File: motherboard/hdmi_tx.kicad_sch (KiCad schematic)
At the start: 38 parts, among them J8 HDMI_A, Q1 2SK3018W, Q2 2SK3018W, Q3 L2N7002WT1G, Q4 2SK3018W, Q5 2SK3018W, Q6 WNM6002-3/TR, Q7 WNM6002-3/TR, Q8 WNM6002-3/TR, Q9 WNM6002-3/TR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

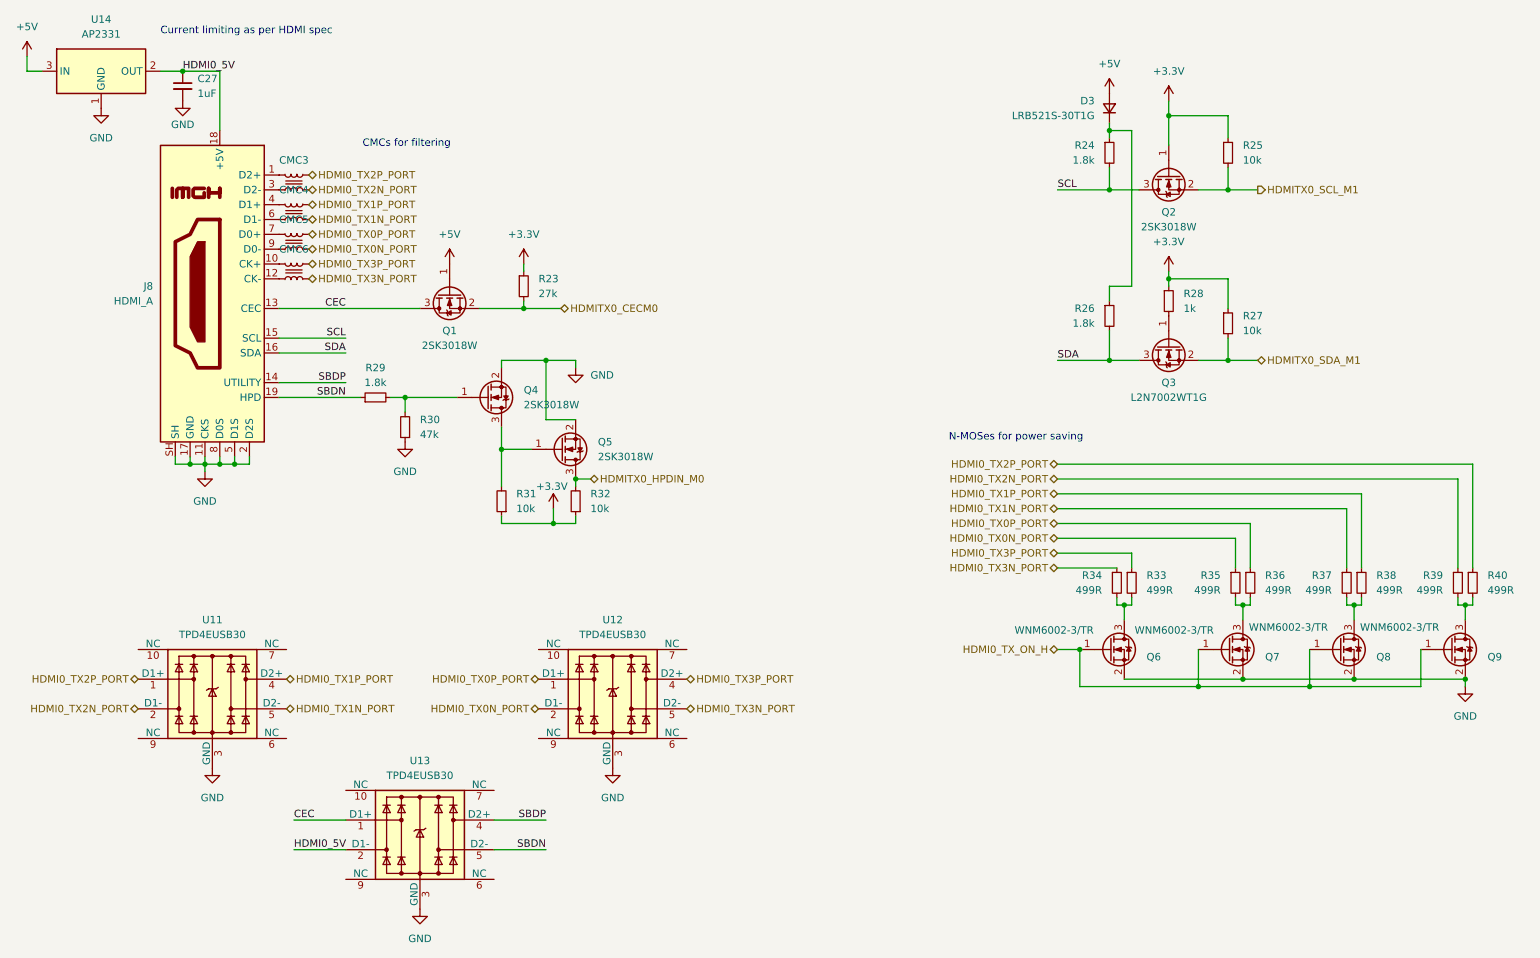
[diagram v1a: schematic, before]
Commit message: synchronizing hierarchical pins
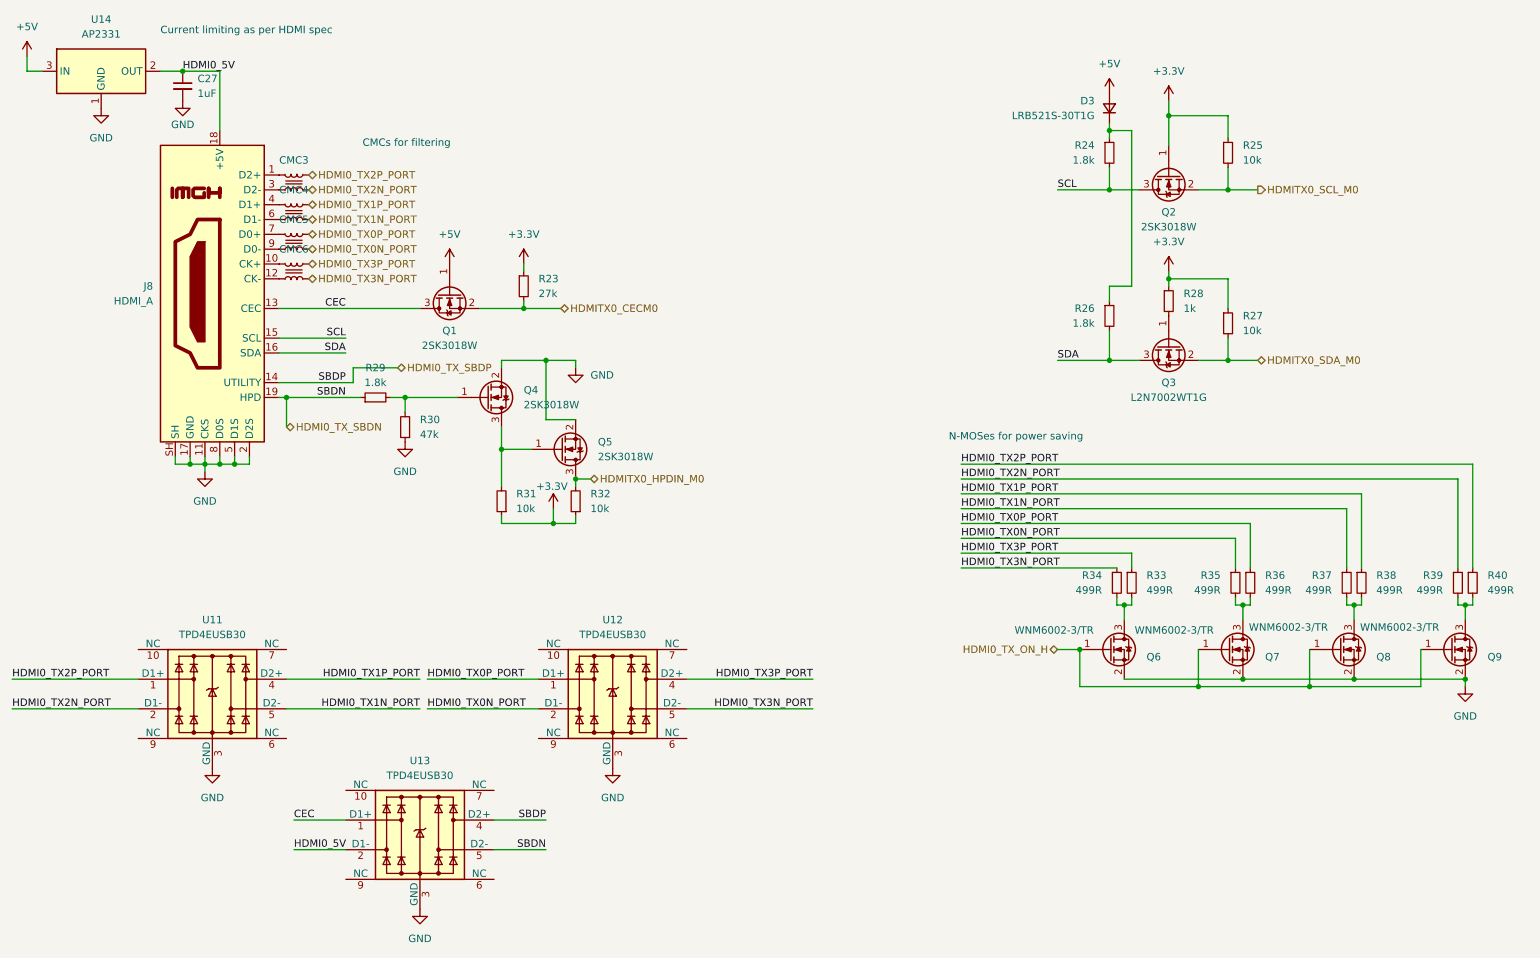
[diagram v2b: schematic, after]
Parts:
- C27: footprint (none) -> Capacitor_SMD:C_0402_1005Metric
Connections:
- net HDMITX0_SCL_M1 renamed HDMITX0_SCL_M0
- net HDMITX0_SDA_M1 renamed HDMITX0_SDA_M0
- net SBDN renamed HDMI0_TX_SBDN
- net SBDP renamed HDMI0_TX_SBDP

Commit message: linked all footprints
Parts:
- D3: footprint (none) -> Diode_SMD:D_SOD-523
- J8: footprint (none) -> Connector_Video:HDMI_A_Molex_208658-1001_Horizontal
- R23, R24, R25, R26, R27, R28, R29, R30, R31, R32, R33, R34, R35, R36, R37, R38, R39, R40: footprint (none) -> Resistor_SMD:R_0402_1005Metric
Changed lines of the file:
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@@
 			)
 		)
-		(property "Footprint" ""
+		(property "Footprint" "Resistor_SMD:R_0402_1005Metric"
 			(at 269.24 128.27 0)
 			(effects
@@
 			)
 		)
-		(property "Footprint" ""
+		(property "Footprint" "Resistor_SMD:R_0402_1005Metric"
 			(at 208.28 128.27 0)
 			(effects
@@
 			)
 		)
-		(property "Footprint" ""
+		(property "Footprint" "Resistor_SMD:R_0402_1005Metric"
 			(at 81.28 96.52 0)
 			(effects
@@
 			)
 		)
-		(property "Footprint" ""
+		(property "Footprint" "Resistor_SMD:R_0402_1005Metric"
 			(at 207.01 54.61 0)
 			(effects
@@
 			)
 		)
-		(property "Footprint" ""
+		(property "Footprint" "Resistor_SMD:R_0402_1005Metric"
 			(at 86.36 101.6 0)
 			(effects
@@
 			)
 		)
-		(property "Footprint" ""
+		(property "Footprint" "Resistor_SMD:R_0402_1005Metric"
 			(at 217.17 80.01 0)
 			(effects
@@
 			)
 		)
-		(property "Footprint" ""
+		(property "Footprint" "Resistor_SMD:R_0402_1005Metric"
 			(at 228.6 128.27 0)
 			(effects
@@
 			)
 		)
-		(property "Footprint" ""
+		(property "Footprint" "Connector_Video:HDMI_A_Molex_208658-1001_Horizontal"
 			(at 53.975 78.74 0)
 			(effects
@@
 			)
 		)
-		(property "Footprint" ""
+		(property "Footprint" "Resistor_SMD:R_0402_1005Metric"
 			(at 231.14 128.27 0)
 			(effects
@@
 			)
 		)
-		(property "Footprint" ""
+		(property "Footprint" "Resistor_SMD:R_0402_1005Metric"
 			(at 227.33 83.82 0)
 			(effects
@@
 			)
 		)
-		(property "Footprint" ""
+		(property "Footprint" "Resistor_SMD:R_0402_1005Metric"
 			(at 102.87 114.3 0)
 			(effects
@@
 			)
 		)
-		(property "Footprint" ""
+		(property "Footprint" "Resistor_SMD:R_0402_1005Metric"
 			(at 227.33 54.61 0)
 			(effects
@@
 			)
 		)
-		(property "Footprint" ""
+		(property "Footprint" "Resistor_SMD:R_0402_1005Metric"
 			(at 115.57 114.3 0)
 			(effects
@@
 			)
 		)
-		(property "Footprint" ""
+		(property "Footprint" "Resistor_SMD:R_0402_1005Metric"
 			(at 247.65 128.27 0)
 			(effects
@@
 			)
 		)
-		(property "Footprint" ""
+		(property "Footprint" "Resistor_SMD:R_0402_1005Metric"
 			(at 210.82 128.27 0)
 			(effects
@@
 			)
 		)
-		(property "Footprint" ""
+		(property "Footprint" "Resistor_SMD:R_0402_1005Metric"
 			(at 207.01 82.55 0)
 			(effects
@@
 			)
 		)
-		(property "Footprint" ""
+		(property "Footprint" "Diode_SMD:D_SOD-523"
 			(at 207.01 46.99 90)
 			(effects
@@
 			)
 		)
-		(property "Footprint" ""
+		(property "Footprint" "Resistor_SMD:R_0402_1005Metric"
 			(at 250.19 128.27 0)
 			(effects
@@
 			)
 		)
-		(property "Footprint" ""
+		(property "Footprint" "Resistor_SMD:R_0402_1005Metric"
 			(at 266.7 128.27 0)
 			(effects
@@
 			)
 		)
-		(property "Footprint" ""
+		(property "Footprint" "Resistor_SMD:R_0402_1005Metric"
 			(at 106.68 77.47 0)
 			(effects

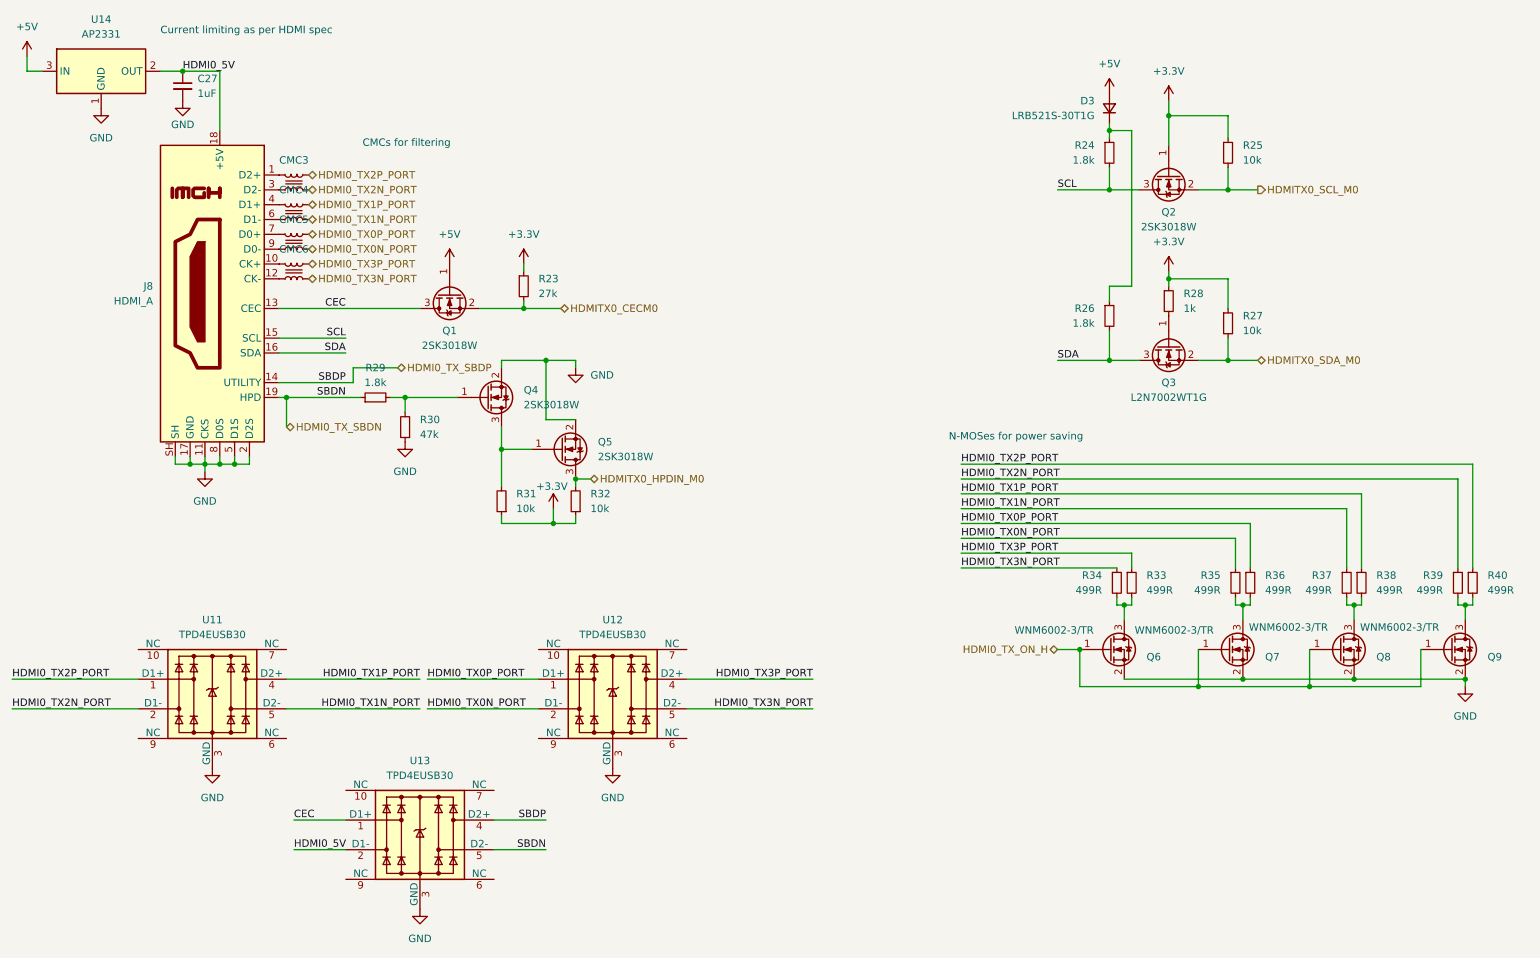
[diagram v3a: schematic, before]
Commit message: cost optimizations for jlc
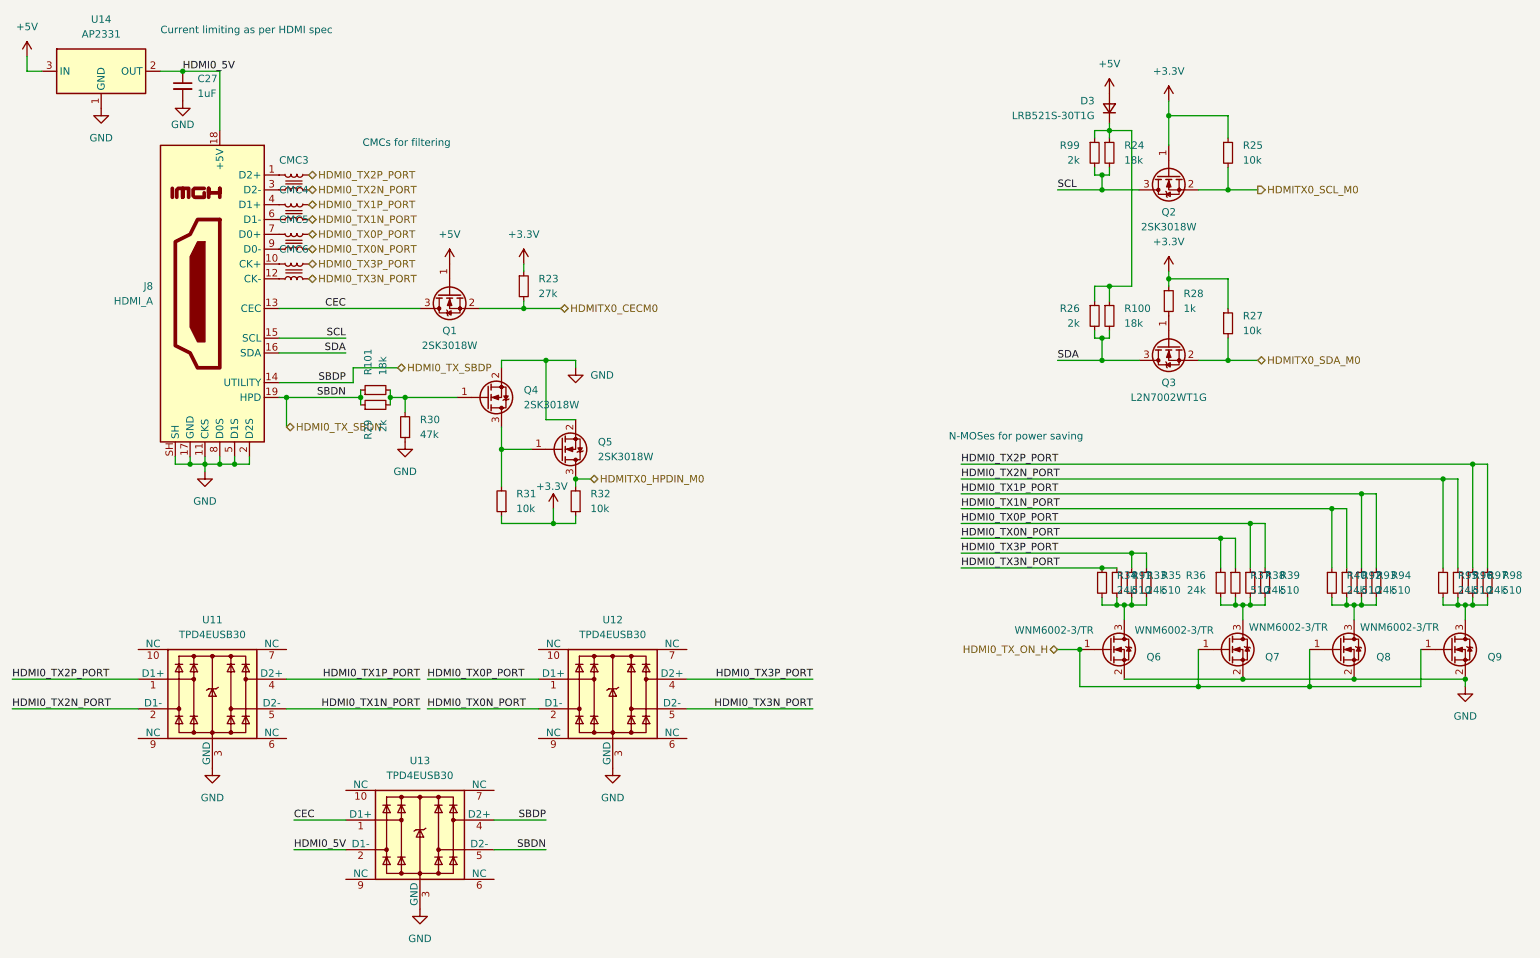
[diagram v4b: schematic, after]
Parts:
- added R100, R101: 18k, Resistor_SMD:R_0402_1005Metric, symbol Device:R_Small
- added R91, R92, R94, R96, R98: 510, Resistor_SMD:R_0402_1005Metric, symbol Device:R_Small
- added R93, R95, R97: 24k, Resistor_SMD:R_0402_1005Metric, symbol Device:R_Small
- added R99: 2k, Resistor_SMD:R_0402_1005Metric, symbol Device:R_Small
- R24: value 1.8k -> 18k
- R26, R29: value 1.8k -> 2k
- R33, R34, R36, R38, R40: value 499R -> 24k
- R35, R37, R39: value 499R -> 510
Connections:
- net HDMI0_TX0N_PORT: now also R36.1, R37.1; no longer R35.1
- net HDMI0_TX0P_PORT: now also R38.1, R39.1; no longer R36.1
- net HDMI0_TX1N_PORT: now also R40.1, R92.1; no longer R37.1
- net HDMI0_TX1P_PORT: now also R93.1, R94.1; no longer R38.1
- net HDMI0_TX2N_PORT: now also R95.1, R96.1; no longer R39.1
- net HDMI0_TX2P_PORT: now also R97.1, R98.1; no longer R40.1
- net HDMI0_TX3N_PORT: now also R91.1
- net HDMI0_TX3P_PORT: now also R35.1
- net HDMI0_TX_SBDN: now also R101.1
- net SCL: now also R99.2
- net SDA: now also R100.2
- net at Q6.3 (D), R33.2, R34.2: now also R35.2, R91.2
- net at Q4.1 (G), R29.2, R30.2: now also R101.2
- net at D3.1 (K), R24.1, R26.1: now also R100.1, R99.1
- net at Q7.3 (D), R36.2: now also R37.2, R38.2, R39.2; no longer R35.2
- new net: Q9.3 (D), R95.2, R96.2, R97.2, R98.2
- new net: Q8.3 (D), R40.2, R92.2, R93.2, R94.2
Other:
- moved on the sheet: R34
